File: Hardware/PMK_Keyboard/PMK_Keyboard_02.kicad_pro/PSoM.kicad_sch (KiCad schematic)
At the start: 12 parts, among them J201 PSoM_ESP32S2_Carrier_Board, J202 PSoM_ESP32S2_Carrier_Board

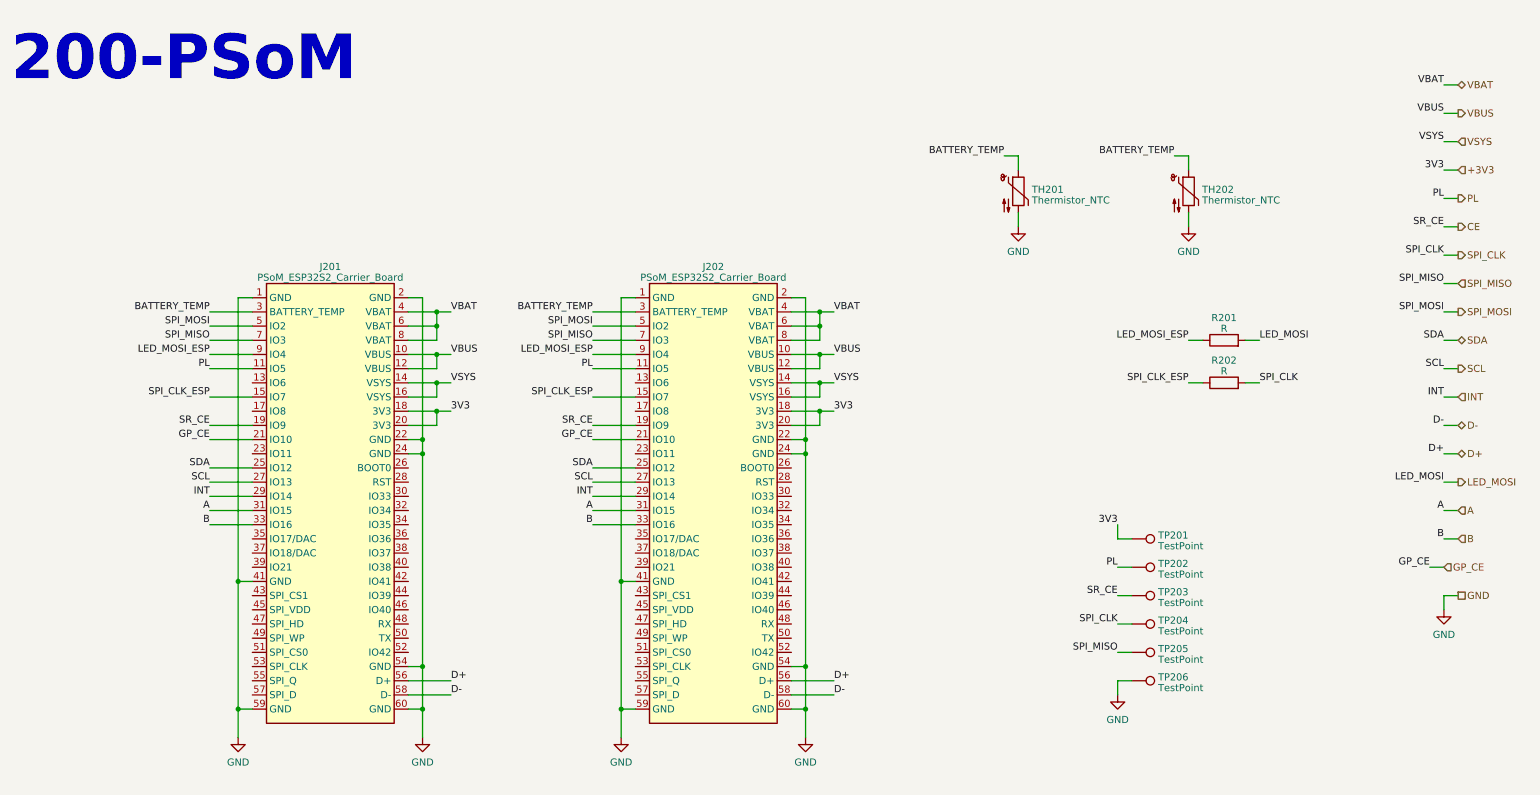
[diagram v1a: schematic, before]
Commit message: added module connector
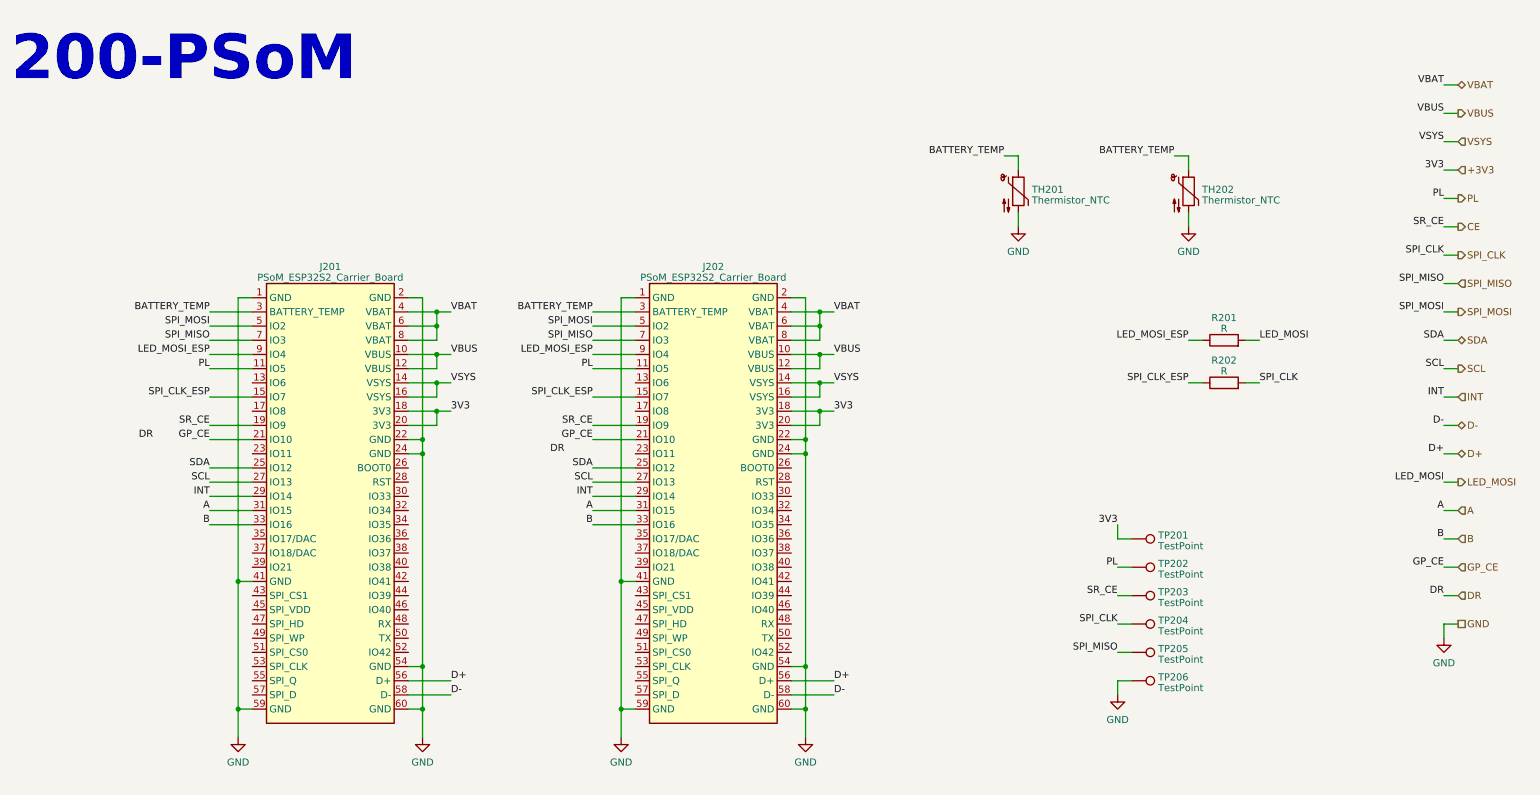
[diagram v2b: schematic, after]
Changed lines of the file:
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@@
+	(wire
+		(pts
+			(xy 271.78 121.92) (xy 274.32 121.92)
+		)
+		(stroke
+			(width 0)
+			(type default)
+		)
+	)
 	(wire
 		(pts
@@
 	(wire
 		(pts
-			(xy 271.78 124.46) (xy 271.78 121.92)
+			(xy 271.78 129.54) (xy 271.78 127)
 		)
 		(stroke
@@
 	(wire
 		(pts
-			(xy 269.24 116.84) (xy 271.78 116.84)
+			(xy 271.78 116.84) (xy 274.32 116.84)
 		)
 		(stroke
@@
 	(wire
 		(pts
-			(xy 271.78 121.92) (xy 274.32 121.92)
+			(xy 271.78 127) (xy 274.32 127)
 		)
 		(stroke
@@
 		)
 	)
+	(label "DR"
+		(at 114.3 96.52 180)
+		(fields_autoplaced yes)
+		(effects
+			(font
+				(size 1.27 1.27)
+			)
+			(justify right bottom)
+		)
+	)
 	(label "D-"
 		(at 271.78 91.44 180)
@@
 		)
 	)
+	(label "DR"
+		(at 40.64 93.98 180)
+		(fields_autoplaced yes)
+		(effects
+			(font
+				(size 1.27 1.27)
+			)
+			(justify right bottom)
+		)
+	)
 	(label "D+"
 		(at 93.98 137.16 0)
@@
 	)
 	(label "GP_CE"
-		(at 269.24 116.84 180)
+		(at 271.78 116.84 180)
 		(fields_autoplaced yes)
 		(effects
@@
 			)
 			(justify left bottom)
+		)
+	)
+	(label "DR"
+		(at 271.78 121.92 180)
+		(fields_autoplaced yes)
+		(effects
+			(font
+				(size 1.27 1.27)
+			)
+			(justify right bottom)
 		)
 	)
@@
 		)
 	)
+	(hierarchical_label "DR"
+		(shape input)
+		(at 274.32 121.92 0)
+		(fields_autoplaced yes)
+		(effects
+			(font
+				(size 1.27 1.27)
+			)
+			(justify left)
+		)
+	)
 	(hierarchical_label "CE"
 		(shape output)
@@
 	(hierarchical_label "GND"
 		(shape passive)
-		(at 274.32 121.92 0)
+		(at 274.32 127 0)
 		(fields_autoplaced yes)
 		(effects
@@
 	(hierarchical_label "GP_CE"
 		(shape input)
-		(at 271.78 116.84 0)
+		(at 274.32 116.84 0)
 		(fields_autoplaced yes)
 		(effects
@@
 	(symbol
 		(lib_id "power:GND")
-		(at 271.78 124.46 0)
+		(at 271.78 129.54 0)
 		(unit 1)
 		(exclude_from_sim no)
@@
 		(fields_autoplaced yes)
 		(property "Reference" "#PWR0203"
-			(at 271.78 130.81 0)
+			(at 271.78 135.89 0)
 			(effects
 				(font
@@
 		)
 		(property "Value" "GND"
-			(at 271.78 128.9034 0)
+			(at 271.78 133.9834 0)
 			(effects
 				(font
@@
 		)
 		(property "Footprint" ""
-			(at 271.78 124.46 0)
+			(at 271.78 129.54 0)
 			(effects
 				(font
@@
 		)
 		(property "Datasheet" ""
-			(at 271.78 124.46 0)
+			(at 271.78 129.54 0)
 			(effects
 				(font
@@
 		)
 		(property "Description" ""
-			(at 271.78 124.46 0)
-			(effects
-				(font
+			(at 271.78 129.54 0)
+			(effects
+				(font

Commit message: Schematic 02 done
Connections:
- net A: now also J201.29 (IO14), J202.29 (IO14); no longer J201.31 (IO15), J202.31 (IO15)
- net B: now also J201.31 (IO15), J202.31 (IO15); no longer J201.33 (IO16), J202.33 (IO16)
- net CE: now also J201.11 (IO5), J202.11 (IO5); no longer J201.19 (IO9), J202.19 (IO9)
- net DR: now also J201.25 (IO12), J202.25 (IO12)
- net GP_CE: now also J201.27 (IO13), J202.27 (IO13); no longer J201.21 (IO10), J202.21 (IO10)
- net INT: now also J201.17 (IO8), J202.17 (IO8); no longer J201.29 (IO14), J202.29 (IO14)
- net LED_MOSI_ESP: now also J201.33 (IO16), J202.33 (IO16); no longer J201.9 (IO4), J202.9 (IO4)
- net PL: now also J201.23 (IO11), J202.23 (IO11); no longer J201.11 (IO5), J202.11 (IO5)
- net SCL: now also J201.15 (IO7), J202.15 (IO7); no longer J201.27 (IO13), J202.27 (IO13)
- net SDA: now also J201.13 (IO6), J202.13 (IO6); no longer J201.25 (IO12), J202.25 (IO12)
- net SPI_CLK_ESP: now also J201.9 (IO4), J202.9 (IO4); no longer J201.15 (IO7), J202.15 (IO7)
- no-connect marks 0 -> 4

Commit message: working on schematic
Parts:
- added TP206: RX, TestPoint:TestPoint_Pad_D1.5mm, symbol Connector:TestPoint
- added TP207: TX, TestPoint:TestPoint_Pad_D1.5mm, symbol Connector:TestPoint
- TP201: value TestPoint -> 3V3
- TP202: value TestPoint -> PL
- TP203: value TestPoint -> SR_CE
- TP204: value TestPoint -> SPI_CLK
- TP205: value TestPoint -> MISO
- TP208: renamed from TP206; value TestPoint -> GND
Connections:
- net RX: now reaches J202.48 (RX)
- net RX: now also J201.48 (RX), TP206.1
- net TX: now reaches J202.50 (TX)
- net TX: now also J201.50 (TX), TP207.1
- no-connect marks 4 -> 50
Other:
- moved on the sheet: TP208

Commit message: working on routing
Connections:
- net A renamed DB_A
- net B renamed DB_B
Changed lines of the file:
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@@
 		)
 	)
-	(label "A"
+	(label "DB_A"
 		(at 271.78 106.68 180)
 		(fields_autoplaced yes)
@@
 		)
 	)
-	(label "B"
+	(label "DB_B"
 		(at 119.38 106.68 180)
 		(fields_autoplaced yes)
@@
 		)
 	)
-	(label "B"
+	(label "DB_B"
 		(at 271.78 111.76 180)
 		(fields_autoplaced yes)
@@
 		)
 	)
-	(label "B"
+	(label "DB_B"
 		(at 50.8 106.68 180)
 		(fields_autoplaced yes)
@@
 		)
 	)
-	(label "A"
+	(label "DB_A"
 		(at 50.8 104.14 180)
 		(fields_autoplaced yes)
@@
 		)
 	)
-	(label "A"
+	(label "DB_A"
 		(at 119.38 104.14 180)
 		(fields_autoplaced yes)
@@
 		)
 	)
-	(hierarchical_label "B"
+	(hierarchical_label "DB_B"
 		(shape input)
 		(at 274.32 111.76 0)
@@
 		)
 	)
-	(hierarchical_label "A"
+	(hierarchical_label "DB_A"
 		(shape input)
 		(at 274.32 106.68 0)

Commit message: routing ongoing
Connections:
- net INT is gone; now on net PL: J201.17 (IO8), J202.17 (IO8)
- net DB_A: now also J201.31 (IO15), J202.31 (IO15); no longer J201.29 (IO14), J202.29 (IO14)
- net DB_B: now also J201.33 (IO16), J202.33 (IO16); no longer J201.31 (IO15), J202.31 (IO15)
- net DR: now also J201.21 (IO10), J202.21 (IO10); no longer J201.25 (IO12), J202.25 (IO12)
- net GP_CE: now also J201.23 (IO11), J202.23 (IO11); no longer J201.27 (IO13), J202.27 (IO13)
- net LED_MOSI_ESP: now also J201.39 (IO21), J202.39 (IO21); no longer J201.33 (IO16), J202.33 (IO16)
- net PL: no longer J201.23 (IO11), J202.23 (IO11)
- net CE renamed SR_CE
- new net GPIO1: J201.25 (IO12), J202.25 (IO12)
- new net GPIO2: J201.27 (IO13), J202.27 (IO13)
- new net GPIO3: J201.29 (IO14), J202.29 (IO14)
- no-connect marks 50 -> 46

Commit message: routing almost done
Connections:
- net DB_A: now also J201.33 (IO16), J202.33 (IO16); no longer J201.31 (IO15), J202.31 (IO15)
- net DB_B: now also J201.31 (IO15), J202.31 (IO15); no longer J201.33 (IO16), J202.33 (IO16)
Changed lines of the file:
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@@
 	)
 	(label "DB_B"
-		(at 50.8 109.22 180)
+		(at 50.8 106.68 180)
 		(fields_autoplaced yes)
 		(effects
@@
 	)
 	(label "DB_A"
-		(at 50.8 106.68 180)
+		(at 50.8 109.22 180)
 		(fields_autoplaced yes)
 		(effects
@@
 	)
 	(label "DB_B"
-		(at 121.92 109.22 180)
+		(at 121.92 106.68 180)
 		(fields_autoplaced yes)
 		(effects
@@
 	)
 	(label "DB_A"
-		(at 121.92 106.68 180)
-		(fields_autoplaced yes)
-		(effects
+		(at 121.92 109.22 180)
+		(fields_autoplaced yes)
+		(effects
